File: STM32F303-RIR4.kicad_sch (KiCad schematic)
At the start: 34 parts, among them J0 CN7, J1 CN10, J101 LCC, J102 LCC, J103 S4 S3 S2 S1 SC, J104 MA MB NA NB, J105 - 12V +, J106 Servo 4, J107 Servo 3, J108 Servo 2, J109 Servo 1, J110 B1 C B2, U101 SN65HVD1050, U102 LM358, U103 TBD62064AFG, U104 TC4428, U105 TC4428, U106 G3VM-61VY4, U107 G3VM-61VY4

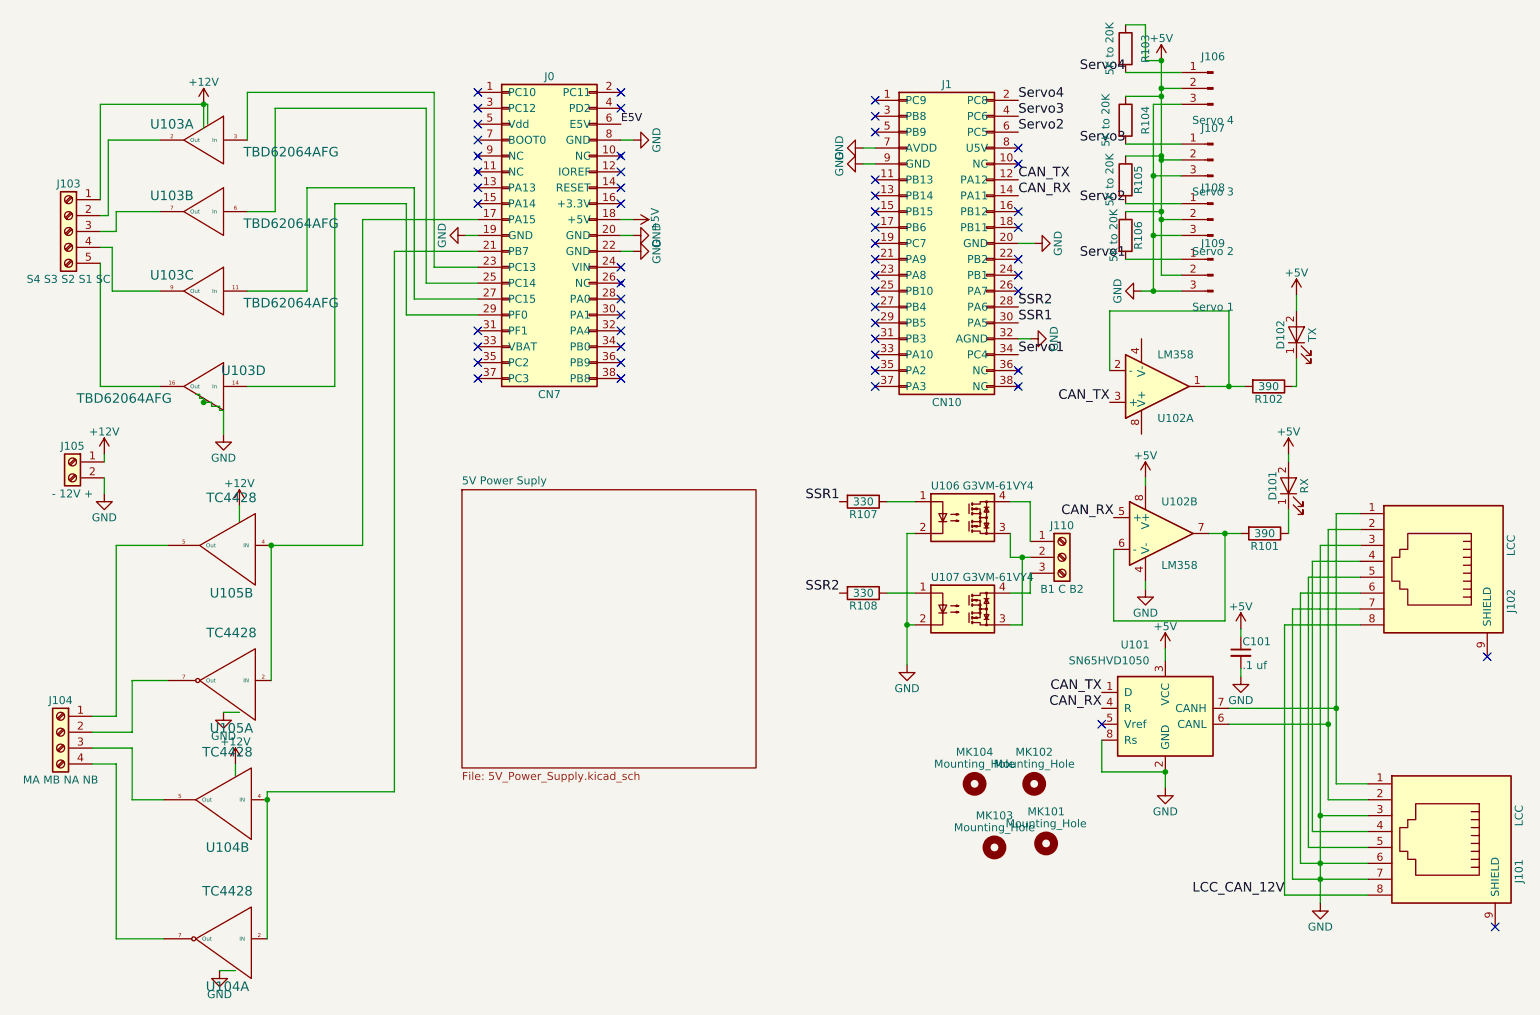
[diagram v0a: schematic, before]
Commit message: Completed 5V power supply.
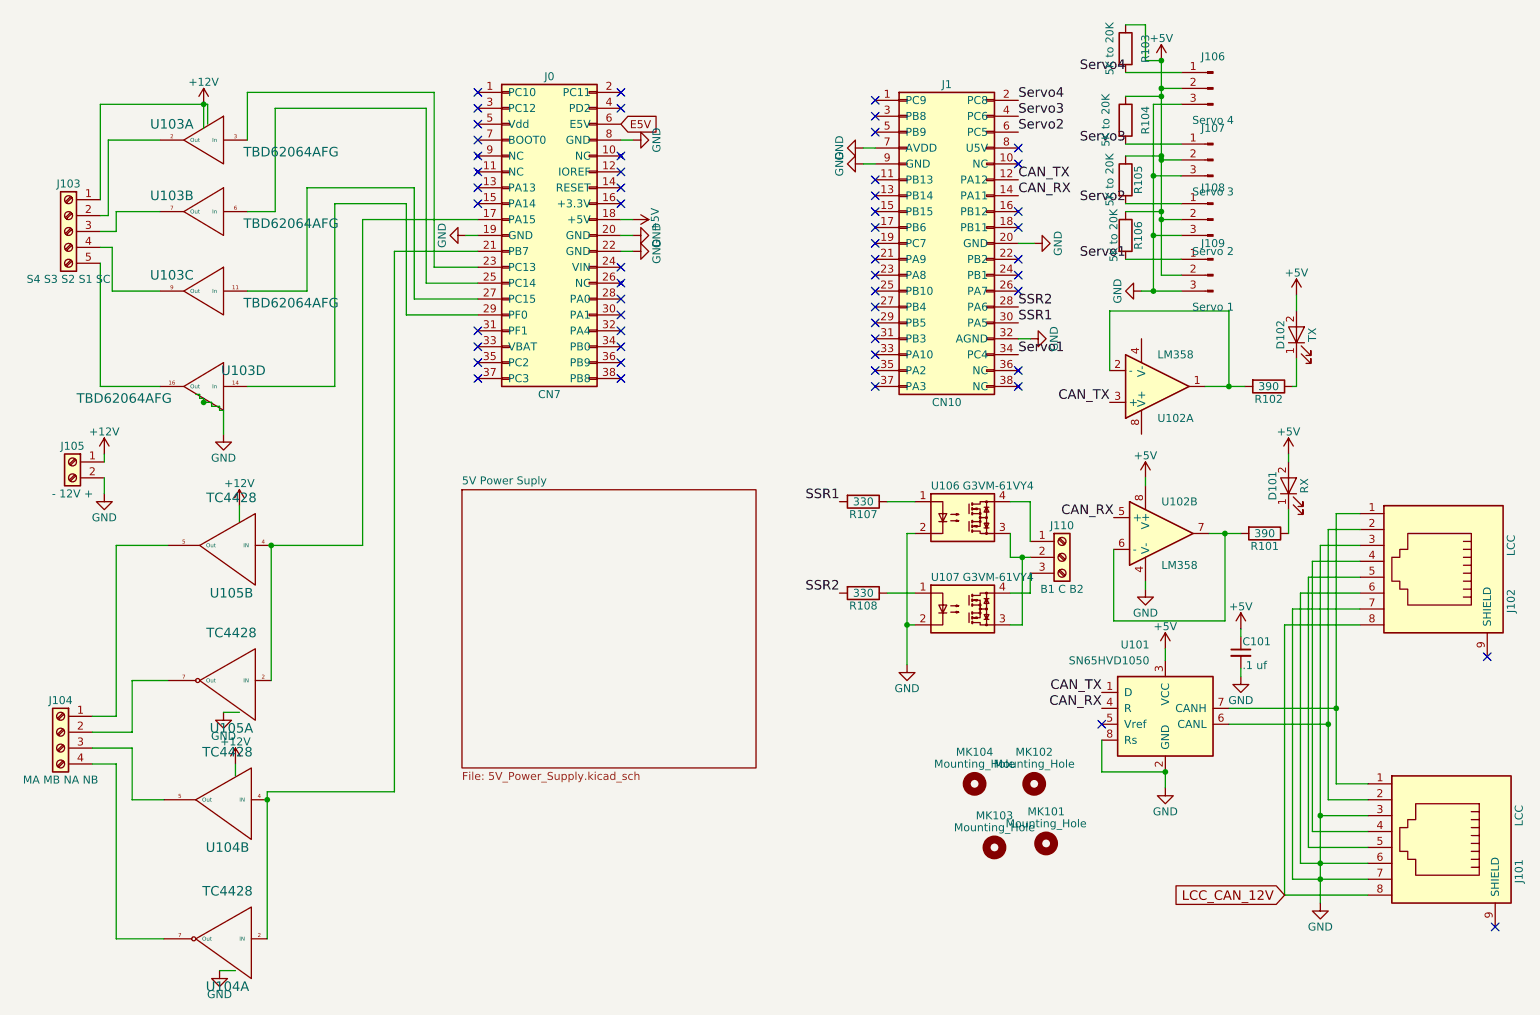
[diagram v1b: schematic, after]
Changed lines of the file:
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@@
     (effects (font (size 1.524 1.524)) (justify left bottom))
-  )
-  (label "E5V" (at 107.315 36.83 0)
-    (effects (font (size 1.27 1.27)) (justify left bottom))
   )
   (label "SSR2" (at 170.815 66.04 0)
@@
     (effects (font (size 1.524 1.524)) (justify right bottom))
   )
-  (label "LCC_CAN_12V" (at 213.36 160.02 180)
-    (effects (font (size 1.524 1.524)) (justify right bottom))
-  )
   (label "Servo4" (at 187.96 28.575 180)
     (effects (font (size 1.524 1.524)) (justify right bottom))
@@
   (label "Servo2" (at 170.815 38.1 0)
     (effects (font (size 1.524 1.524)) (justify left bottom))
+  )
+  (global_label "E5V" (shape input) (at 107.315 36.83 0) (fields_autoplaced)
+    (effects (font (size 1.27 1.27)) (justify left))
+    (property "Intersheet References" "${INTERSHEET_REFS}" (id 0) (at 113.0863 36.7506 0)
+      (effects (font (size 1.27 1.27)) (justify left) hide)
+    )
+  )
+  (global_label "LCC_CAN_12V" (shape input) (at 213.36 160.02 180) (fields_autoplaced)
+    (effects (font (size 1.524 1.524)) (justify right))
+    (property "Intersheet References" "${INTERSHEET_REFS}" (id 0) (at 195.3311 159.9248 0)
+      (effects (font (size 1.524 1.524)) (justify right) hide)
+    )
   )
   (symbol (lib_id "stm32Morpho:CN7") (at 94.615 54.61 0) (unit 1)
@@
     )
     (path "/a1eed654-048f-4954-87cf-ae733d8334dc/56845fec-bf70-4243-9bcd-8767275d7958"
-      (reference "#PWR?") (unit 1) (value "GND") (footprint "")
+      (reference "#PWR0101") (unit 1) (value "GND") (footprint "")
     )
     (path "/00000000-0000-0000-0000-0000642b2d14"
       (reference "C101") (unit 1) (value ".1 uf") (footprint "Capacitors_SMD:C_0603")
     )
+    (path "/a1eed654-048f-4954-87cf-ae733d8334dc/a58ccb51-ffd5-494e-ac83-e76d44ab95b0"
+      (reference "C201") (unit 1) (value "10uf") (footprint "Capacitor_SMD:C_1206_3216Metric")
+    )
+    (path "/a1eed654-048f-4954-87cf-ae733d8334dc/fb852148-4ed3-4072-a526-60a7e3ef5821"
+      (reference "C202") (unit 1) (value "22uf 6.3V") (footprint "Capacitor_SMD:C_1206_3216Metric")
+    )
+    (path "/a1eed654-048f-4954-87cf-ae733d8334dc/7358b296-84f4-43dc-98cc-99e446c7913b"
+      (reference "C203") (unit 1) (value "220uf 20% 10V") (footprint "Capacitor_SMD:CP_Elec_6.3x7.7")
+    )
     (path "/00000000-0000-0000-0000-0000642c5ee3"
       (reference "D101") (unit 1) (value "RX") (footprint "LEDs:LED_0603")
@@
       (reference "D102") (unit 1) (value "TX") (footprint "LEDs:LED_0603")
     )
+    (path "/a1eed654-048f-4954-87cf-ae733d8334dc/e792b142-cd67-403a-8f40-4cdb88ded2a5"
+      (reference "D201") (unit 1) (value "SK23TR") (footprint "Diode_SMD:D_SMB")
+    )
     (path "/00000000-0000-0000-0000-0000642ae579"
       (reference "J0") (unit 1) (value "CN7") (footprint "stm32Morpho:ST_MorfoHeader")
@@
       (reference "J110") (unit 1) (value "B1 C B2") (footprint "Terminal_Blocks:TerminalBlock_Pheonix_MPT-2.54mm_3pol")
     )
+    (path "/a1eed654-048f-4954-87cf-ae733d8334dc/707c1437-ab9e-4b8b-ada6-9d928dfd766c"
+      (reference "L201") (unit 1) (value "47uh") (footprint "inductors:SDR1307A470K")
+    )
     (path "/00000000-0000-0000-0000-0000642b400b"
       (reference "MK101") (unit 1) (value "Mounting_Hole") (footprint "Mounting_Holes:MountingHole_3.2mm_M3")
@@
     )
     (path "/a1eed654-048f-4954-87cf-ae733d8334dc/0152b6c9-1845-4945-a0c9-cd5369d0ec4c"
-      (reference "U?") (unit 1) (value "AP1509-50") (footprint "Package_SO:SOIC-8_3.9x4.9mm_P1.27mm")
-    )
-  )
+      (reference "U201") (unit 1) (value "AP1509-50") (footprint "Package_SO:SOIC-8_3.9x4.9mm_P1.27mm")
+    )
+  )
